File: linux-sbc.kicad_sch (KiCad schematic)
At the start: 7 parts

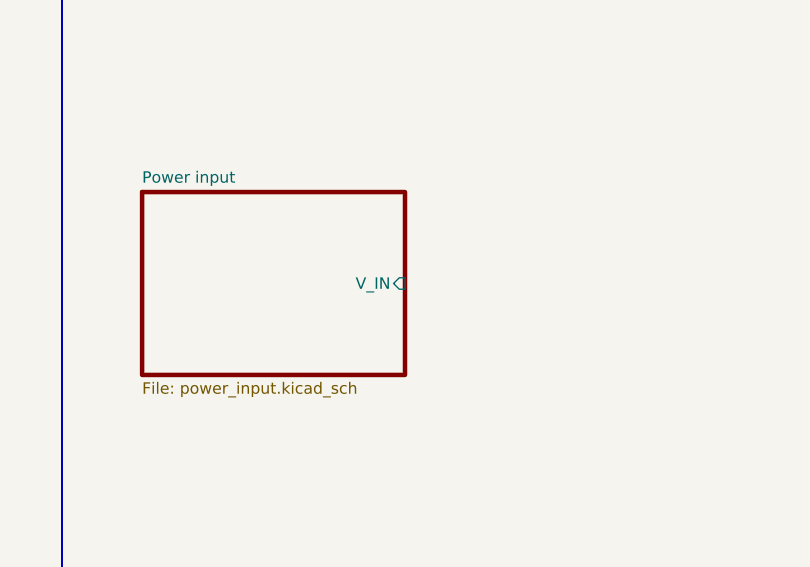
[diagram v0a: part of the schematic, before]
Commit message: Fill BOM for power input sheet
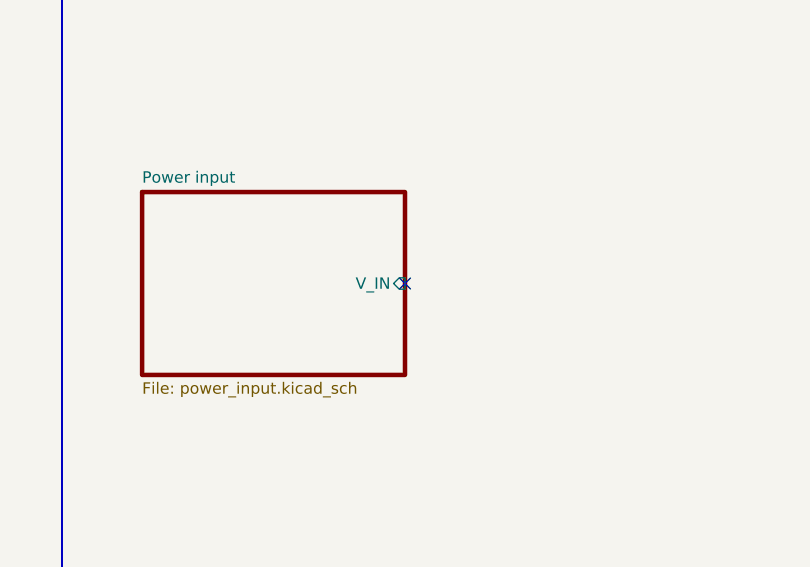
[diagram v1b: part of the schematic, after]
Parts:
- H101, H102, H103, H104: MPN - -> (none); Manufacturer - -> (none)
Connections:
- no-connect marks 0 -> 1

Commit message: Rework intro and power input sheets
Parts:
- added D101: XCEZ30V,L3XHF, Diode_SMD:D_SOD-523, symbol Device:D_Zener
- added J101: Molex Mini-fit Jr, Connector_Molex:Molex_Mini-Fit_Jr_5569-08A2_2x04_P4.20mm_Horizontal, symbol Connector_Generic:Conn_02x02_Odd_Even
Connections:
- net CHASSIS: now also D101.2 (A)
- new net Power input/V_IN+: D101.1 (K), J101.2 (Pin_2), J101.4 (Pin_4)
- new net Power input/V_IN-: J101.1 (Pin_1), J101.3 (Pin_3)
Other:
- sheet Power input ports: added V_IN+, V_IN-, V_SYS; removed V_IN
- note added: "12 - 24 V input ± 10%"
- moved on the sheet: FID101, FID102, FID103, H101, H102, H103, H104

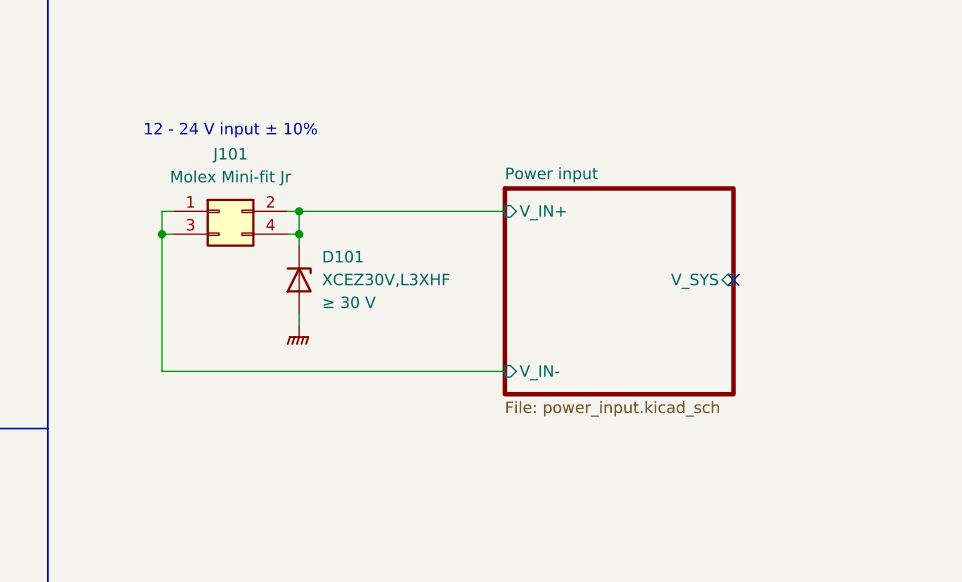
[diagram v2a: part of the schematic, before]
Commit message: Change power input TVS to bidir
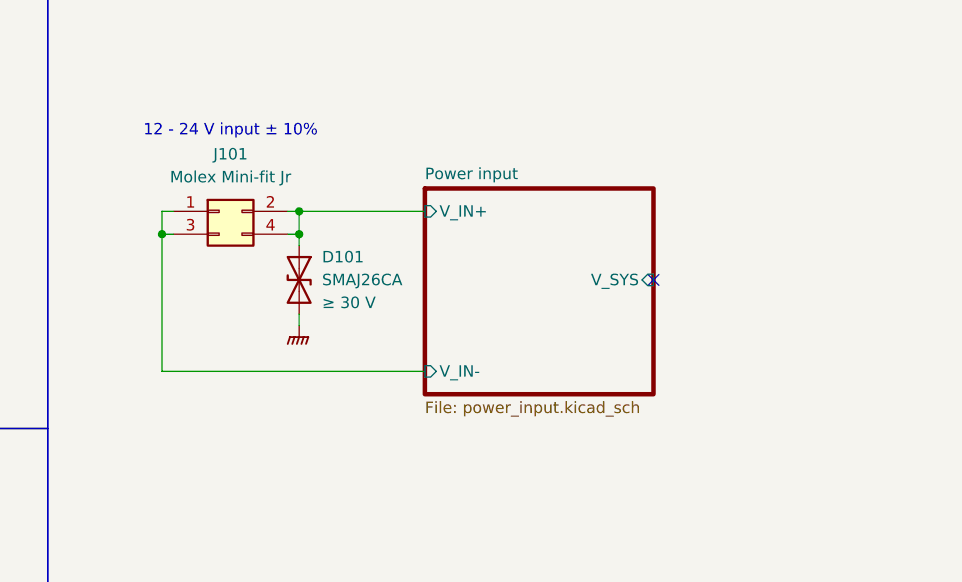
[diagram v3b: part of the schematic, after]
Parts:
- D101: value XCEZ30V,L3XHF -> SMAJ26CA; footprint Diode_SMD:D_SOD-523 -> Diode_SMD:D_SMA; symbol Device:D_Zener -> Device:D_TVS; DigiKey Part Number 264-XCEZ30VL3XHFCT-ND -> 732-SMAJ26CACT-ND; MPN XCEZ30V,L3XHF -> SMAJ26CA; Manufacturer Toshiba Semiconductor and Storage -> Würth Elektronik
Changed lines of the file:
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@@
 	)
 	(no_connect
-		(at 215.9 96.52)
+		(at 207.01 96.52)
 	)
 	(wire
@@
 	(wire
 		(pts
-			(xy 152.4 106.68) (xy 190.5 106.68)
+			(xy 152.4 106.68) (xy 181.61 106.68)
 		)
 		(stroke
@@
 	(wire
 		(pts
-			(xy 167.64 88.9) (xy 190.5 88.9)
+			(xy 167.64 88.9) (xy 181.61 88.9)
 		)
 		(stroke
@@
 	)
 	(symbol
-		(lib_id "Device:D_Zener")
+		(lib_id "Device:D_TVS")
 		(at 167.64 96.52 270)
 		(unit 1)
@@
 			)
 		)
-		(property "Value" "XCEZ30V,L3XHF"
+		(property "Value" "SMAJ26CA"
 			(at 170.18 96.52 90)
 			(effects
@@
 			)
 		)
-		(property "Footprint" "Diode_SMD:D_SOD-523"
+		(property "Footprint" "Diode_SMD:D_SMA"
 			(at 167.64 96.52 0)
 			(effects
@@
 			)
 		)
-		(property "Datasheet" "https://www.st.com/content/ccc/resource/technical/document/datasheet/b0/6e/bc/89/3c/f1/41/b5/CD00283815.pdf/files/CD00283815.pdf/jcr:content/translations/en.CD00283815.pdf"
+		(property "Datasheet" "~"
 			(at 167.64 96.52 0)
 			(effects
@@
 			)
 		)
-		(property "Description" "47.5V Clamp 4A (8/20µs) Ipp Tvs Diode Surface Mount ESC"
+		(property "Description" "Bidirectional transient-voltage-suppression diode"
 			(at 167.64 96.52 0)
 			(effects
@@
 			)
 		)
-		(property "DigiKey Part Number" "264-XCEZ30VL3XHFCT-ND"
+		(property "DigiKey Part Number" "732-SMAJ26CACT-ND"
 			(at 167.64 96.52 90)
 			(effects
@@
 			)
 		)
-		(property "Manufacturer" "Toshiba Semiconductor and Storage"
+		(property "Manufacturer" "Würth Elektronik"
 			(at 167.64 96.52 90)
 			(effects
@@
 			)
 		)
-		(property "MPN" "XCEZ30V,L3XHF"
+		(property "MPN" "SMAJ26CA"
 			(at 167.64 96.52 90)
 			(effects
@@
 	)
 	(sheet
-		(at 190.5 86.36)
+		(at 181.61 86.36)
 		(size 25.4 22.86)
 		(exclude_from_sim no)
@@
 		)
 		(property "Sheetname" "Power input"
-			(at 190.5 85.4746 0)
+			(at 181.61 85.4746 0)
 			(effects
 				(font
@@
 		)
 		(property "Sheetfile" "power_input.kicad_sch"
-			(at 190.5 109.9784 0)
+			(at 181.61 109.9784 0)
 			(effects
 				(font
@@
 		)
 		(pin "V_IN+" input
-			(at 190.5 88.9 180)
+			(at 181.61 88.9 180)
 			(effects
 				(font
@@
 		)
 		(pin "V_IN-" input
-			(at 190.5 106.68 180)
+			(at 181.61 106.68 180)
 			(effects
 				(font
@@
 		)
 		(pin "V_SYS" input
-			(at 215.9 96.52 0)
-			(effects
-				(font
+			(at 207.01 96.52 0)
+			(effects
+				(font

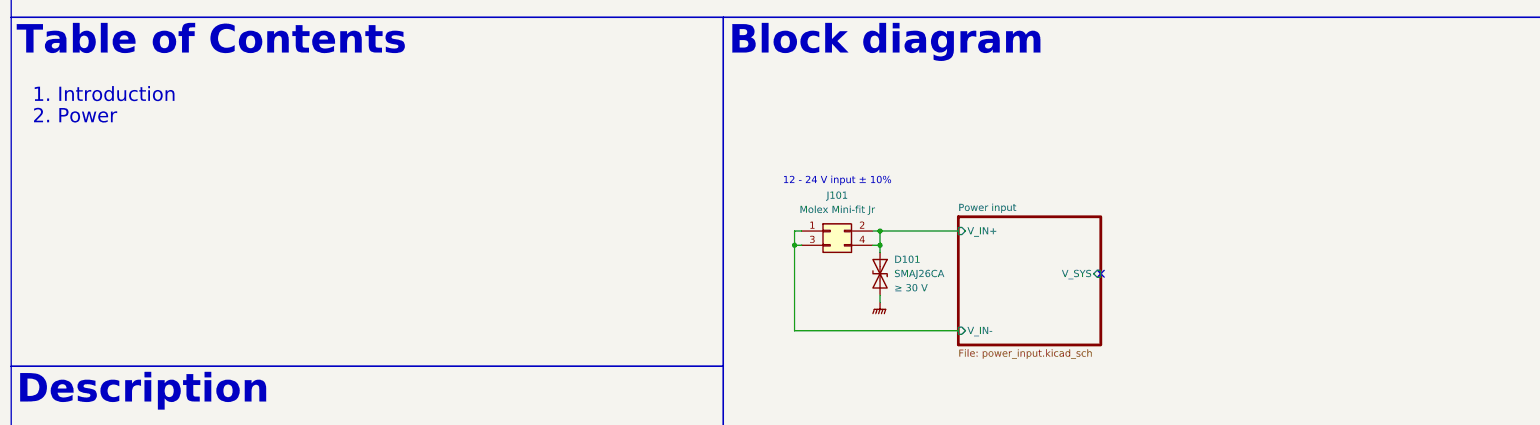
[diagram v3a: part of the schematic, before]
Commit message: Add power generation sheet
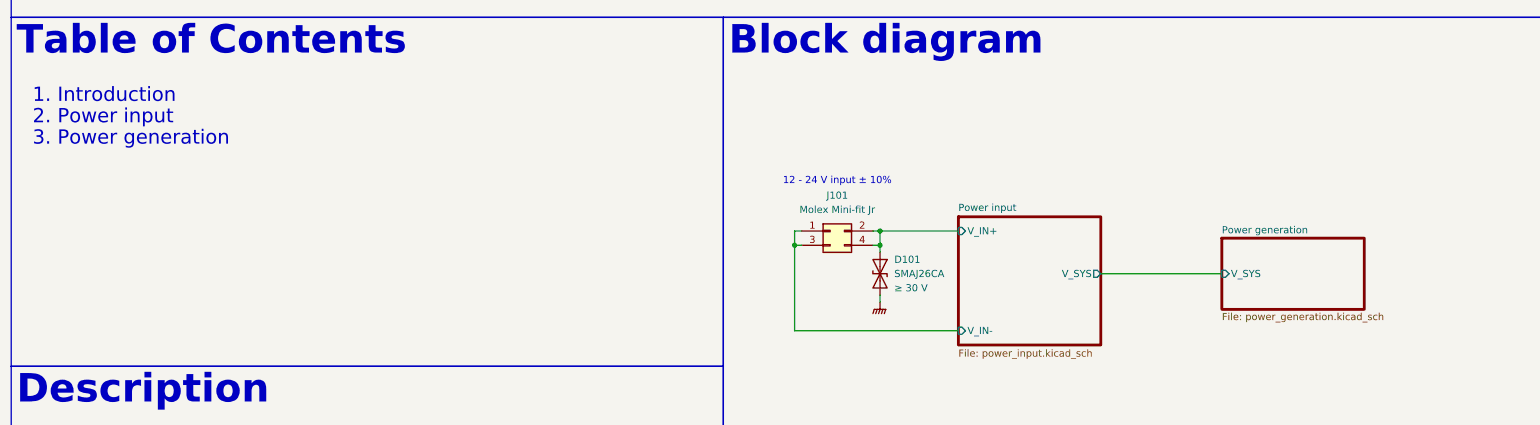
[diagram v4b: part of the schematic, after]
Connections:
- no-connect marks 1 -> 0
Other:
- added sheet Power generation (power_generation.kicad_sch)
- note added: "2. Power input"
- note added: "3. Power generation"
- note removed: "2. Power"
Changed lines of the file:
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@@
 		(rev "v0.0.1")
+	)
+	(text "3. Power generation"
+		(exclude_from_sim no)
+		(at 16.51 72.39 0)
+		(effects
+			(font
+				(size 2.54 2.54)
+			)
+			(justify left)
+			(href "#3")
+		)
 	)
 	(text "- Layout comments are in magenta"
@@
 		)
 	)
-	(text "2. Power"
+	(text "2. Power input"
 		(exclude_from_sim no)
 		(at 16.51 68.58 0)
@@
 		(color 0 0 0 0)
 	)
-	(no_connect
-		(at 207.01 96.52)
-	)
 	(wire
 		(pts
@@
 		(pts
 			(xy 153.67 88.9) (xy 152.4 88.9)
+		)
+		(stroke
+			(width 0)
+			(type default)
+		)
+	)
+	(wire
+		(pts
+			(xy 207.01 96.52) (xy 228.6 96.52)
 		)
 		(stroke
@@
 			(width 0.5)
 			(type solid)
-			(color 0 0 0 1)
+			(color 255 255 0 1)
 		)
 		(fill
@@
 			)
 		)
-		(pin "V_SYS" input
+		(pin "V_SYS" output
 			(at 207.01 96.52 0)
 			(effects
@@
 				)
 			)
+		)
+	)
+	(sheet
+		(at 228.6 90.17)
+		(size 25.4 12.7)
+		(exclude_from_sim no)
+		(in_bom yes)
+		(on_board yes)
+		(dnp no)
+		(fields_autoplaced yes)
+		(stroke
+			(width 0.5)
+			(type solid)
+			(color 255 255 0 1)
+		)
+		(fill
+			(color 0 255 0 1.0000)
+		)
+		(property "Sheetname" "Power generation"
+			(at 228.6 89.4584 0)
+			(effects
+				(font
+					(size 1.27 1.27)
+				)
+				(justify left bottom)
+			)
+		)
+		(property "Sheetfile" "power_generation.kicad_sch"
+			(at 228.6 103.4546 0)
+			(effects
+				(font
+					(size 1.27 1.27)
+				)
+				(justify left top)
+			)
+		)
+		(pin "V_SYS" input
+			(at 228.6 96.52 180)
+			(effects
+				(font
+					(size 1.27 1.27)
+				)
+				(justify left)
+			)
+		)
+		(instances
+			(project "linux-sbc"
+				(path "/fa11a02f-8043-4153-ab69-88d766503017"
+					(page "3")
+				)
+			)

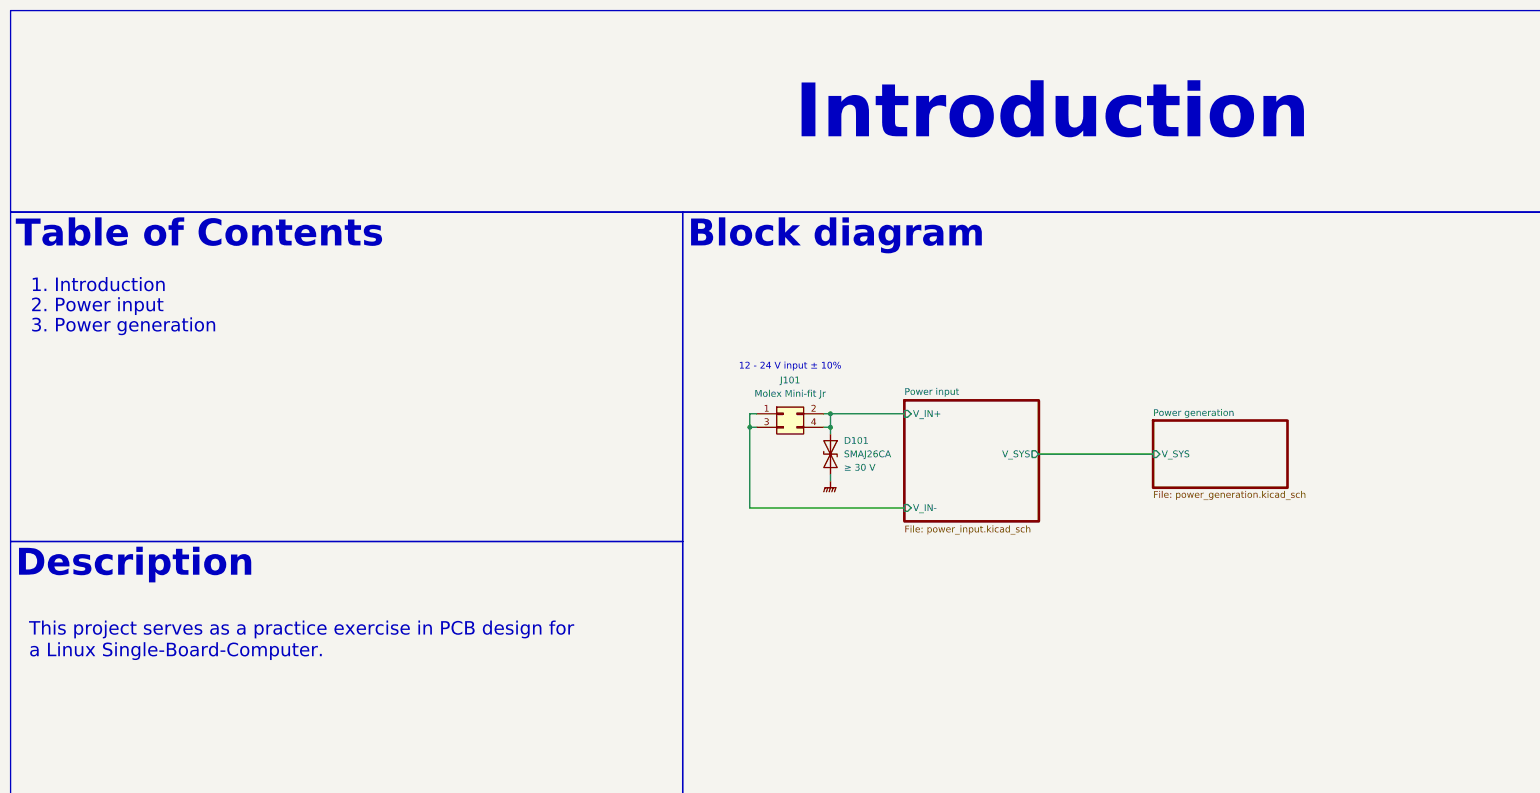
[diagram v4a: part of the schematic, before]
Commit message: Add MPU power generation
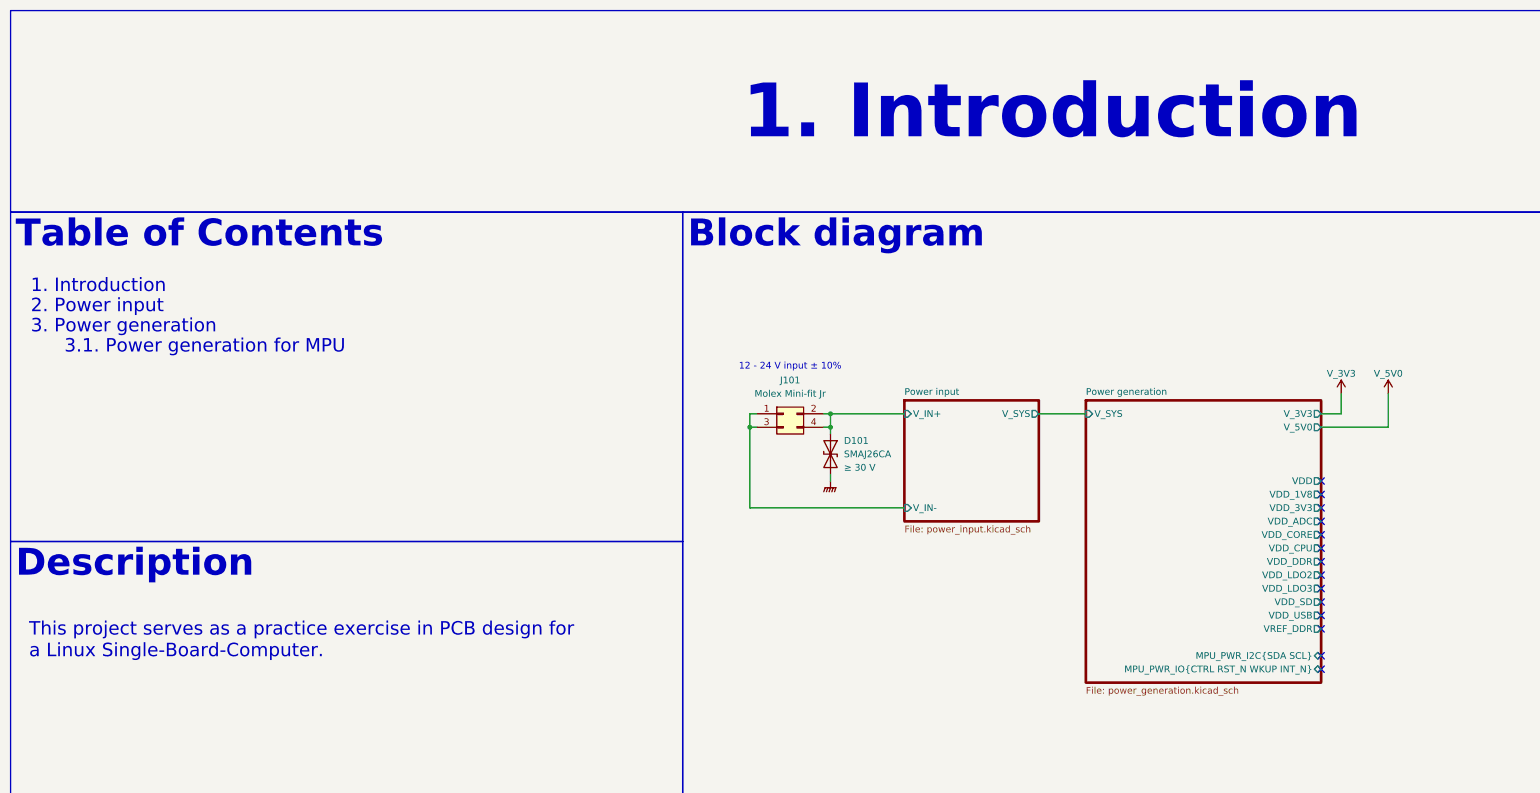
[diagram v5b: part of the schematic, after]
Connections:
- no-connect marks 0 -> 14
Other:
- sheet Power generation ports: added MPU_PWR_I2C{SDA SCL}, MPU_PWR_IO{CTRL RST_N WKUP INT_N}, VDD, VDD_1V8, VDD_3V3, VDD_ADC, VDD_CORE, VDD_CPU, VDD_DDR, VDD_LDO2, VDD_LDO3, VDD_SD, VDD_USB, VREF_DDR, V_3V3, V_5V0; removed none
- note added: "3.1. Power generation for MPU"

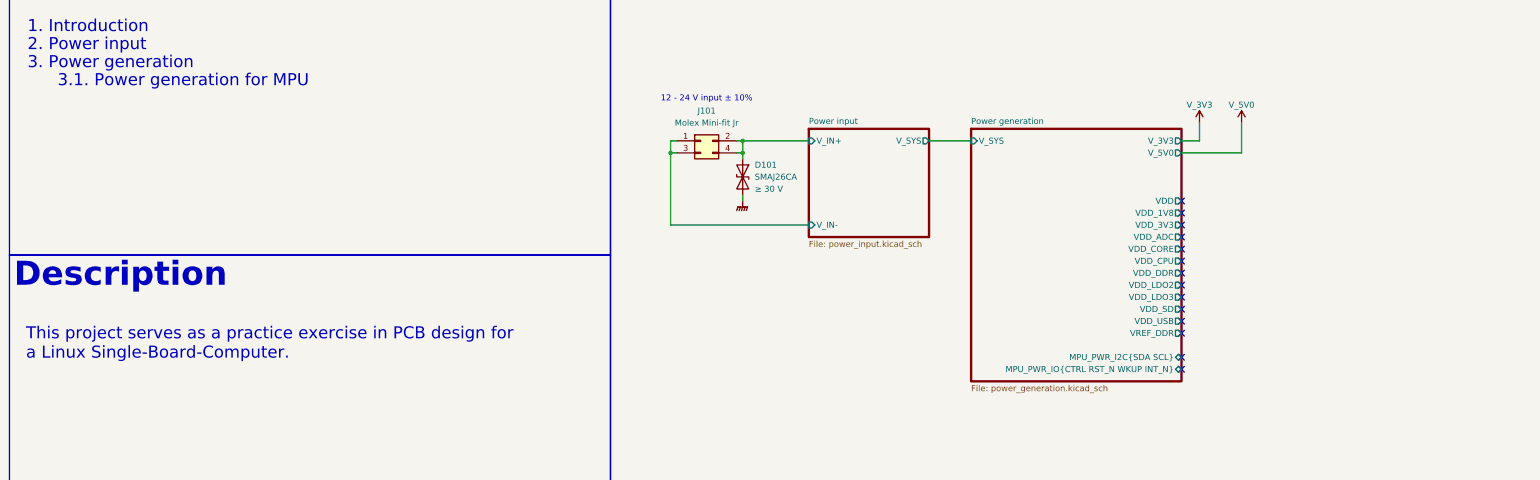
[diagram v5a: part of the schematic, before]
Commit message: Reorganize schema and add MPU
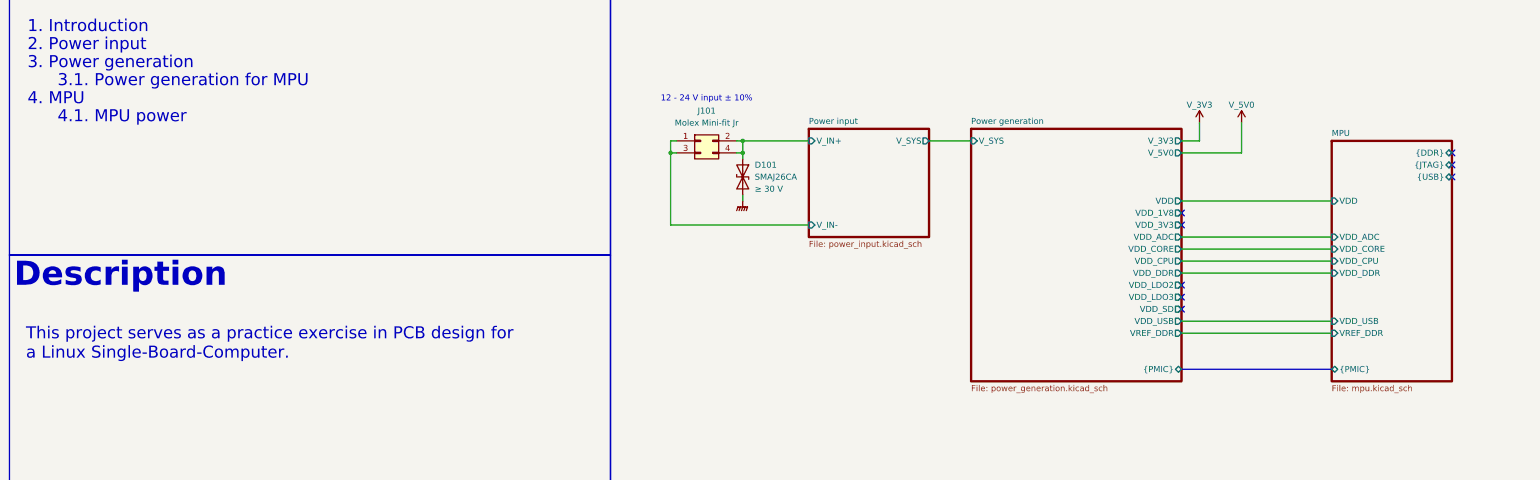
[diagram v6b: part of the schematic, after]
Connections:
- no-connect marks 14 -> 8
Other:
- added sheet MPU (mpu.kicad_sch)
- sheet Power generation ports: added {PMIC}; removed MPU_PWR_I2C{SDA SCL}, MPU_PWR_IO{CTRL RST_N WKUP INT_N}
- note added: "4. MPU"
- note added: "4.1. MPU power"

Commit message: Reorganize schema
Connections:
- no-connect marks 8 -> 10
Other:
- sheet MPU ports: added VDD_1V8, VDD_3V3, VDD_LDO2, VDD_LDO3, VDD_SD; removed VDD, VDD_ADC, VDD_CORE, VDD_CPU, VDD_DDR, VDD_USB
- sheet Power generation ports: added none; removed VDD, VDD_1V8, VDD_3V3, VDD_ADC, VDD_CORE, VDD_CPU, VDD_DDR, VDD_LDO2, VDD_LDO3, VDD_SD, VDD_USB, VREF_DDR, {PMIC}
- note added: "4.1. MPU PMIC"
- note added: "4.2. MPU power"
- note removed: "3.1. Power generation for MPU"
- note removed: "4.1. MPU power"
